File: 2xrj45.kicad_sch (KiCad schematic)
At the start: 33 parts, among them J1 Bus_RJ45_JTH-0024NL, J10 MP_Terminal_M3_THT_7760, J2 Bus_RJ45_JTH-0024NL, J9 MP_Terminal_M3_THT_7760

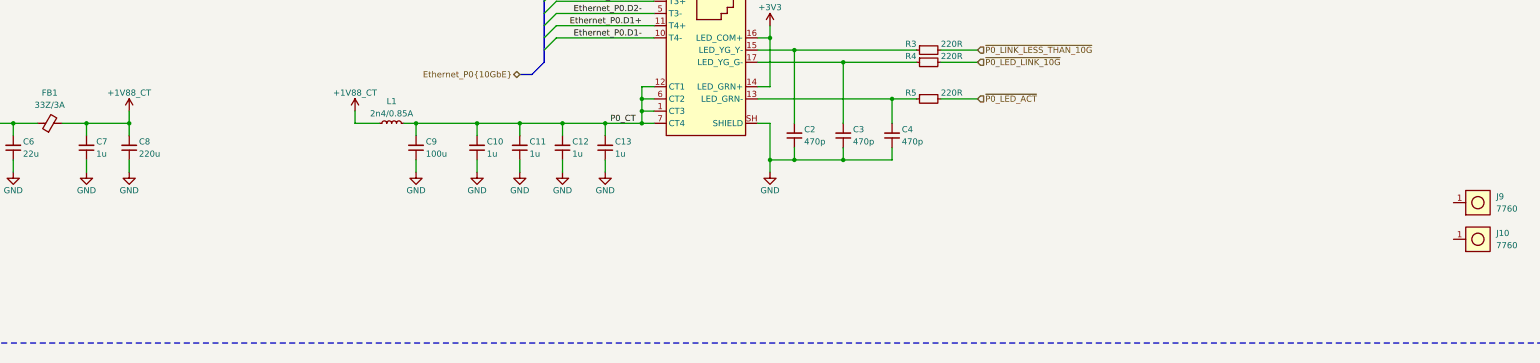
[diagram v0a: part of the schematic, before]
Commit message: [#85196] Clear ERC, minor schematic fixes
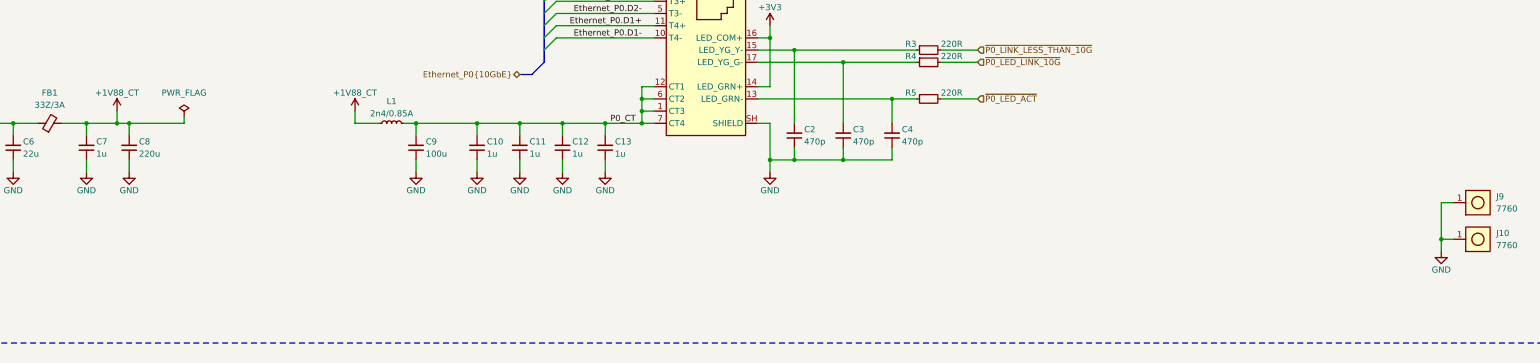
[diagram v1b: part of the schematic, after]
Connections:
- net GND: now also J10.1, J9.1

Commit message: [#85196] Re-annotate schematic
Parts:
- renumbered C2 to C48, C3 to C49, C4 to C50, C5 to C51, C6 to C52, C7 to C53, C8 to C54, C9 to C55, C10 to C56, C11 to C57, C12 to C58, C13 to C59, C14 to C60, C15 to C61, C16 to C62, C17 to C63, C18 to C64, C19 to C65, C20 to C66, C21 to C67, J1 to J3, J9 to J4, J10 to J5, J2 to J6, L1 to L6, L2 to L7, R3 to R36, R4 to R37, R5 to R38, R6 to R39, R7 to R40, R8 to R41
